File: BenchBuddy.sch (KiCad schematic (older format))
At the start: 0 parts

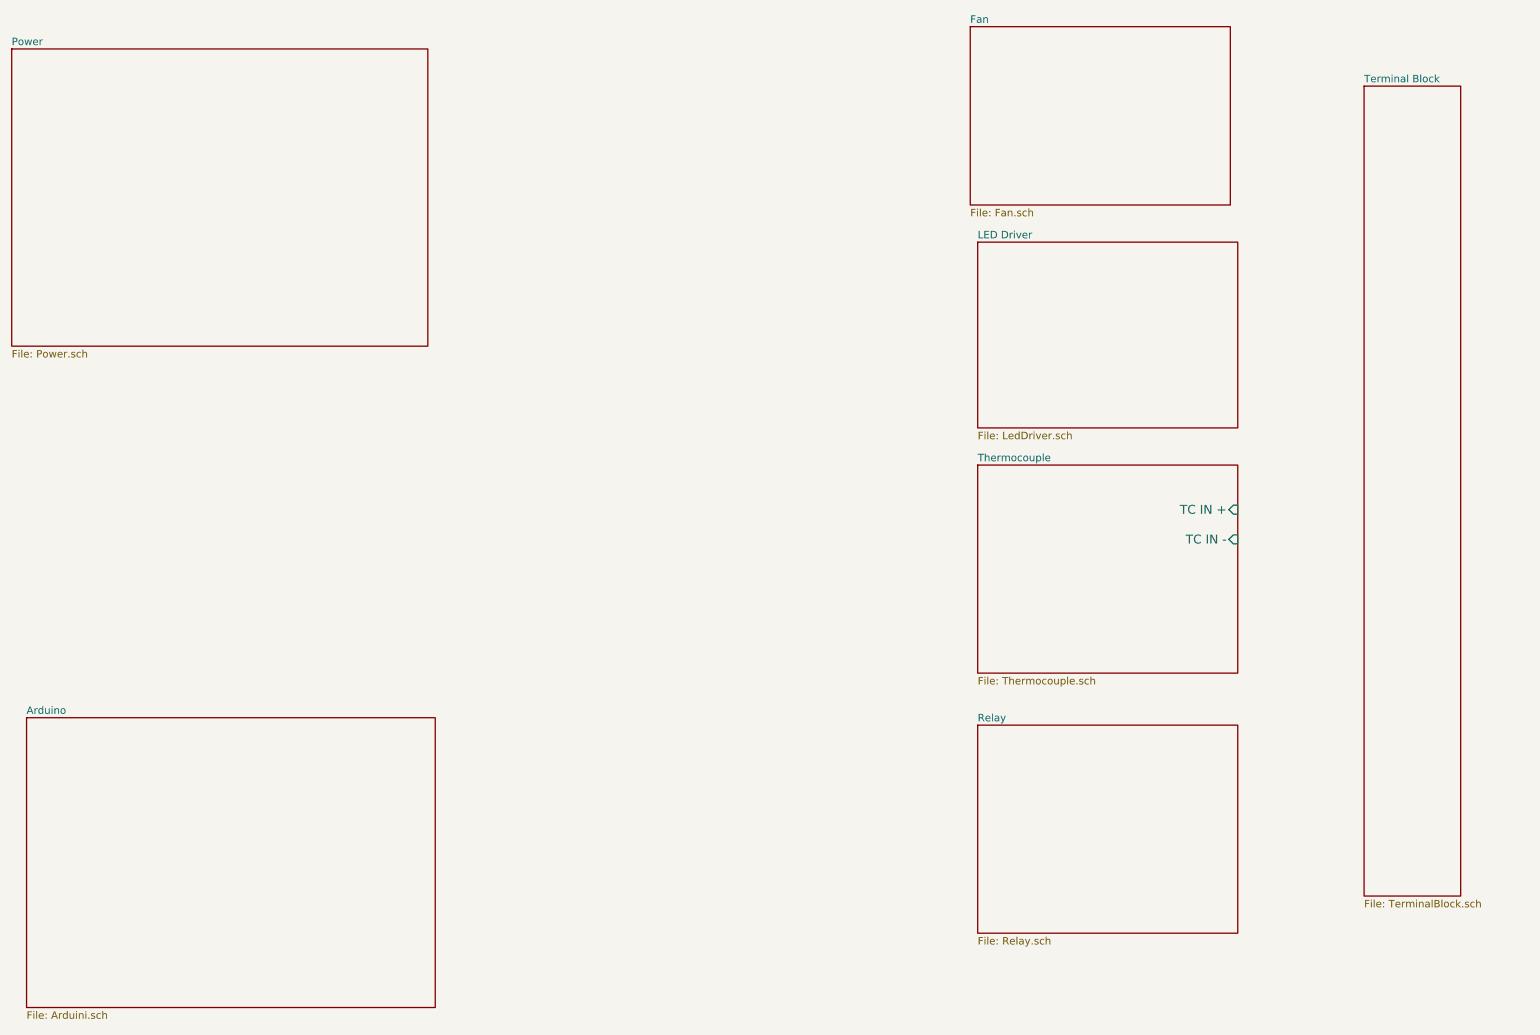
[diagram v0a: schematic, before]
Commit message: Module Inputs & Outputs
Module Inputs and Outputs have been placed on the block diagram sheet
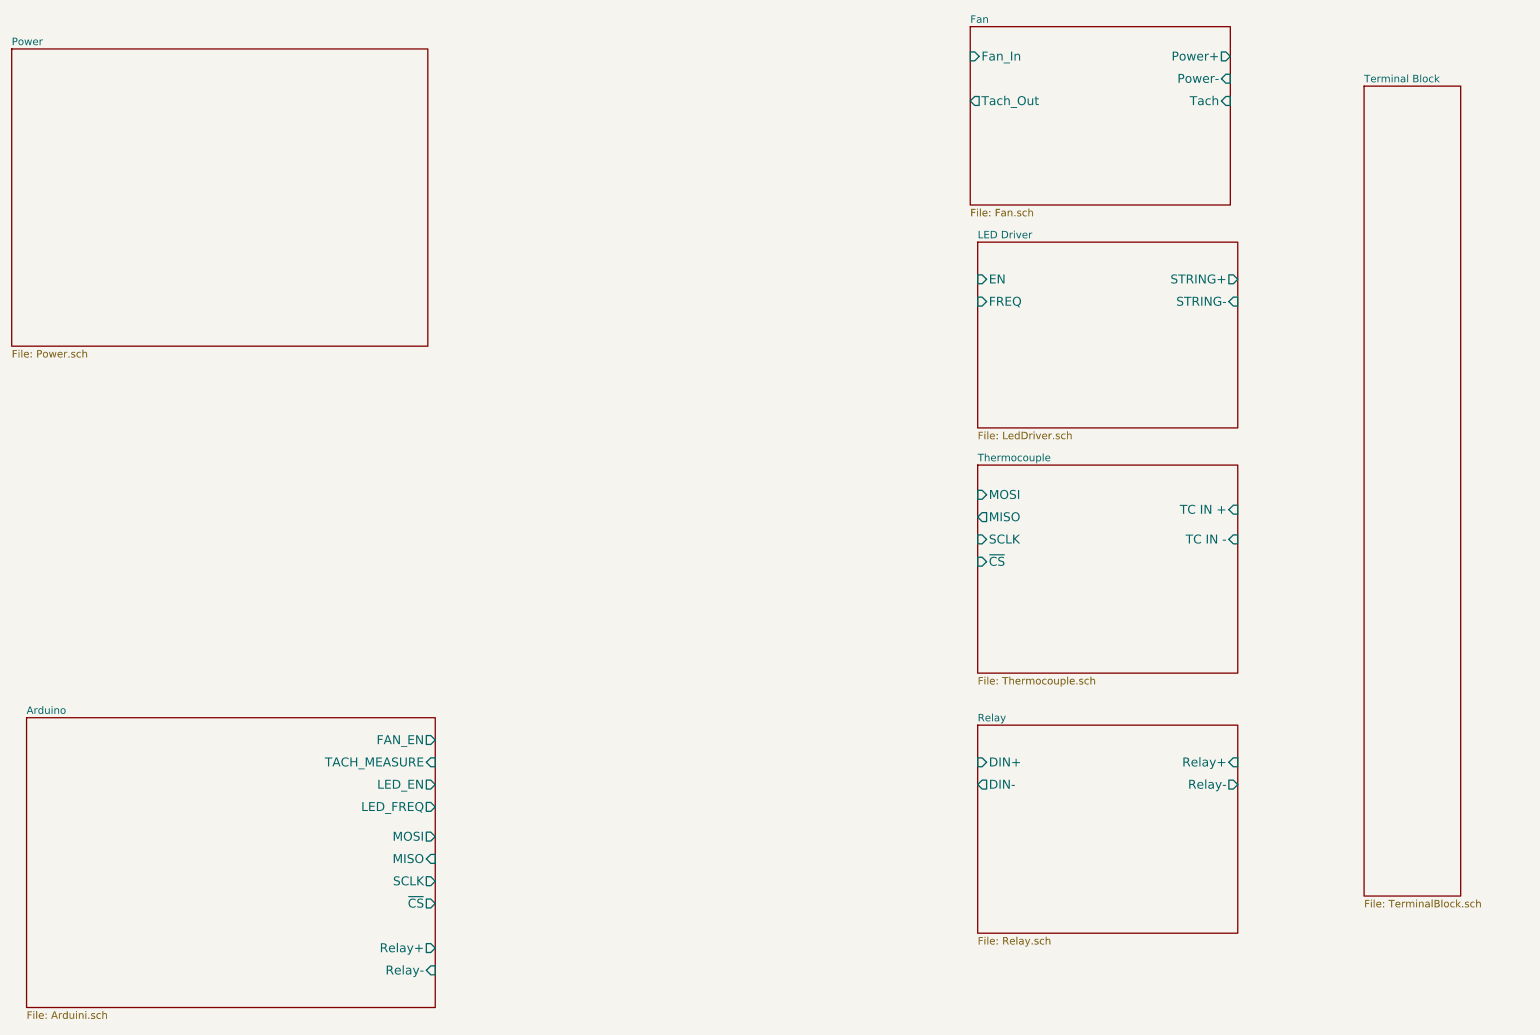
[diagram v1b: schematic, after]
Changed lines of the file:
@@
 $EndDescr
-$Sheet
-S 1250 5300 2750 1950
-U 52326DF6
-F0 "Arduino" 50
-F1 "Arduini.sch" 50
-$EndSheet
 $Sheet
 S 7650 3600 1750 1400
@@
 F2 "TC IN +" I R 9400 3900 60
 F3 "TC IN -" I R 9400 4100 60
+F4 "MOSI" I L 7650 3800 60
+F5 "MISO" O L 7650 3950 60
+F6 "SCLK" I L 7650 4100 60
+F7 "~CS" I L 7650 4250 60
 $EndSheet
 $Sheet
@@
 F0 "Relay" 50
 F1 "Relay.sch" 50
+F2 "DIN+" I L 7650 5600 60
+F3 "DIN-" O L 7650 5750 60
+F4 "Relay+" I R 9400 5600 60
+F5 "Relay-" O R 9400 5750 60
 $EndSheet
 $Sheet
@@
 F0 "LED Driver" 50
 F1 "LedDriver.sch" 50
+F2 "EN" I L 7650 2350 60
+F3 "FREQ" I L 7650 2500 60
+F4 "STRING+" O R 9400 2350 60
+F5 "STRING-" I R 9400 2500 60
 $EndSheet
 $Sheet
@@
 F0 "Fan" 50
 F1 "Fan.sch" 50
+F2 "Power+" O R 9350 850 60
+F3 "Power-" I R 9350 1000 60
+F4 "Tach" I R 9350 1150 60
+F5 "Tach_Out" O L 7600 1150 60
+F6 "Fan_In" I L 7600 850 60
 $EndSheet
 $Sheet
@@
 F1 "TerminalBlock.sch" 50
 $EndSheet
+$Sheet
+S 1250 5300 2750 1950
+U 52326DF6
+F0 "Arduino" 50
+F1 "Arduini.sch" 50
+F2 "Relay+" O R 4000 6850 60
+F3 "Relay-" I R 4000 7000 60
+F4 "MOSI" O R 4000 6100 60
+F5 "MISO" I R 4000 6250 60
+F6 "SCLK" O R 4000 6400 60
+F7 "~CS" O R 4000 6550 60
+F8 "LED_EN" O R 4000 5750 60
+F9 "LED_FREQ" O R 4000 5900 60
+F10 "FAN_EN" O R 4000 5450 60
+F11 "TACH_MEASURE" I R 4000 5600 60
+$EndSheet
 $EndSCHEMATC

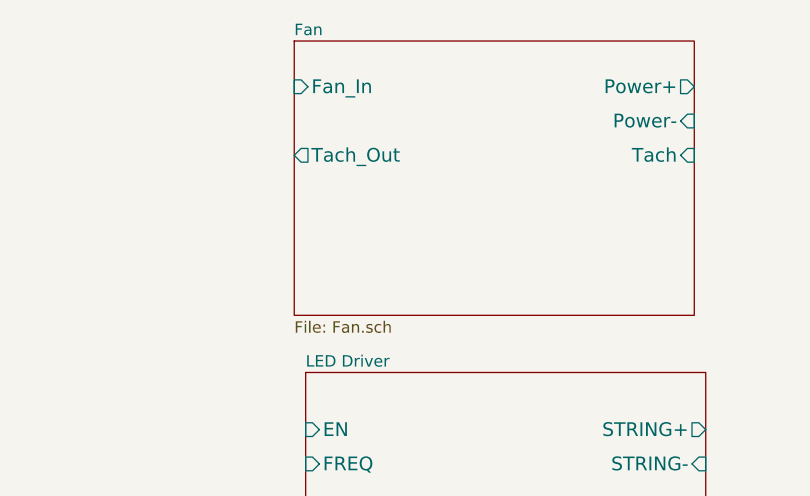
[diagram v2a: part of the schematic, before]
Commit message: Added Fan Schematic
Added generic schematic for fan controller
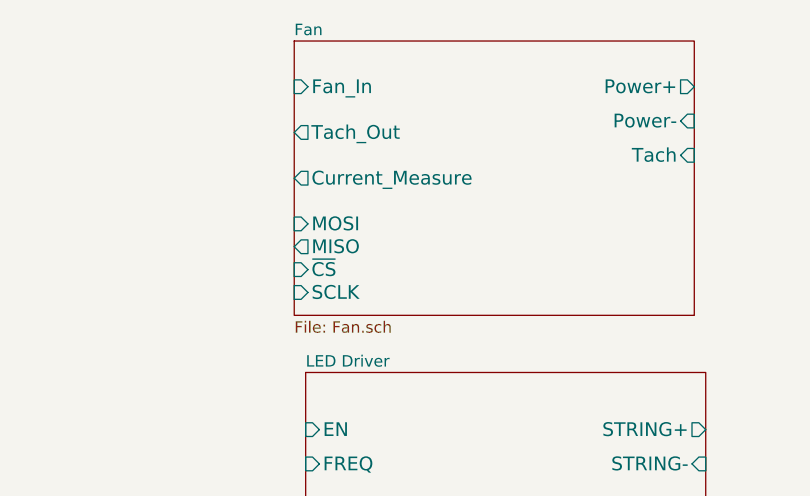
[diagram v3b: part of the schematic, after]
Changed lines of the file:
@@
 F3 "Power-" I R 9350 1000 60
 F4 "Tach" I R 9350 1150 60
-F5 "Tach_Out" O L 7600 1150 60
+F5 "Tach_Out" O L 7600 1050 60
 F6 "Fan_In" I L 7600 850 60
+F7 "Current_Measure" O L 7600 1250 60
+F8 "MOSI" I L 7600 1450 60
+F9 "MISO" O L 7600 1550 60
+F10 "~CS" I L 7600 1650 60
+F11 "SCLK" I L 7600 1750 60
 $EndSheet
 $Sheet

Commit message: Power Filtering & Protection Module
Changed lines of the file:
@@
 $Descr A4 11693 8268
 encoding utf-8
-Sheet 1 8
+Sheet 1 9
 Title ""
 Date "4 oct 2013"
@@
 $EndSheet
 $Sheet
-S 1250 5300 2750 1950
+S 1250 5300 2400 1750
 U 52326DF6
 F0 "Arduino" 50
 F1 "Arduini.sch" 50
-F2 "Relay+" O R 4000 6850 60
-F3 "Relay-" I R 4000 7000 60
-F4 "MOSI" O R 4000 6100 60
-F5 "MISO" I R 4000 6250 60
-F6 "SCLK" O R 4000 6400 60
-F7 "~CS" O R 4000 6550 60
-F8 "LED_EN" O R 4000 5750 60
-F9 "LED_FREQ" O R 4000 5900 60
-F10 "FAN_EN" O R 4000 5450 60
-F11 "TACH_MEASURE" I R 4000 5600 60
+F2 "Relay+" O R 3650 6850 60
+F3 "Relay-" I R 3650 7000 60
+F4 "MOSI" O R 3650 6100 60
+F5 "MISO" I R 3650 6250 60
+F6 "SCLK" O R 3650 6400 60
+F7 "~CS" O R 3650 6550 60
+F8 "LED_EN" O R 3650 5750 60
+F9 "LED_FREQ" O R 3650 5900 60
+F10 "FAN_EN" O R 3650 5450 60
+F11 "TACH_MEASURE" I R 3650 5600 60
+$EndSheet
+$Sheet
+S 4450 2950 2250 2100
+U 524E194C
+F0 "Power Adjustment Monitor" 50
+F1 "PowerAdjustmentMonitor.sch" 50
 $EndSheet
 $EndSCHEMATC
